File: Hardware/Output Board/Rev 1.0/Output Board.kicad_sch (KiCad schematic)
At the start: 85 parts, among them J1 Prog, J2 SD_Card, J3 Audio L, J4 Audio R, J5 VGA, J6 Conn_02x08_Odd_Even, J7 6502 Bus, U1 ICE40UP5K-SG48ITR50, U10 74HC138, U11 74HC138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

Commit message: Output Board schematic complete
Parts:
- C1, C10, C13, C14, C16, C17, C18, C19, C3, C4, C5, C6, C9: footprint Capacitor_SMD:C_0603_1608Metric -> Capacitor_SMD:C_0805_2012Metric; LCSC (none) -> C49678
- C11, C12, C2, C24, C25, C7, C8: footprint Capacitor_SMD:C_0603_1608Metric -> Capacitor_SMD:C_0805_2012Metric; LCSC (none) -> C1779
- C15, C21: footprint Capacitor_SMD:C_0603_1608Metric -> Capacitor_SMD:C_0805_2012Metric; LCSC (none) -> C1733
- C20: value 1u -> 1uF; footprint Capacitor_SMD:C_0603_1608Metric -> Capacitor_SMD:C_0805_2012Metric; LCSC (none) -> C28323
- C22: footprint Capacitor_SMD:C_0603_1608Metric -> Capacitor_SMD:C_0805_2012Metric; LCSC (none) -> C377773
- C23: footprint Capacitor_SMD:C_0603_1608Metric -> Capacitor_SMD:C_0805_2012Metric; LCSC (none) -> C28323
- C26, C27, C28, C29: LCSC (none) -> C1713
- C31: footprint Capacitor_THT:C_Disc_D5.0mm_W2.5mm_P5.00mm -> Capacitor_SMD:C_0805_2012Metric
- J1, J5, JP1: now left out of the parts list
- J2: LCSC (none) -> C569097
- L1: LCSC (none) -> C92959
- R1, R2, R3: footprint Resistor_SMD:R_0603_1608Metric -> Resistor_SMD:R_0805_2012Metric; LCSC (none) -> C17414
- R10, R15: footprint Resistor_SMD:R_0603_1608Metric -> Resistor_SMD:R_0805_2012Metric; LCSC (none) -> C28636
- R11, R18, R26: footprint Resistor_SMD:R_0603_1608Metric -> Resistor_SMD:R_0805_2012Metric; LCSC (none) -> C17746
- R12, R19, R27: footprint Resistor_SMD:R_0603_1608Metric -> Resistor_SMD:R_0805_2012Metric; LCSC (none) -> C17476
- R13, R14, R20, R23, R4, R5, R6, R7, R8, R9: footprint Resistor_SMD:R_0603_1608Metric -> Resistor_SMD:R_0805_2012Metric; LCSC (none) -> C17713
- R16, R22, R28: footprint Resistor_SMD:R_0603_1608Metric -> Resistor_SMD:R_0805_2012Metric; LCSC (none) -> C17516
- R17, R25, R29: footprint Resistor_SMD:R_0603_1608Metric -> Resistor_SMD:R_0805_2012Metric; LCSC (none) -> C17667
- R21, R24: footprint Resistor_SMD:R_0603_1608Metric -> Resistor_SMD:R_0805_2012Metric; LCSC (none) -> C17837
- U1: LCSC (none) -> C2889329
- U10: footprint Package_DIP:DIP-16_W7.62mm_Socket_LongPads -> Package_SO:SOIC-16_3.9x9.9mm_P1.27mm
- U2: LCSC (none) -> C176912
- U3: LCSC (none) -> C2655473
- U4: LCSC (none) -> C543078
- U5: LCSC (none) -> C7859
- U6: LCSC (none) -> C146242
- U7: LCSC (none) -> C2456211
- U8: LCSC (none) -> C500759
- U9: LCSC (none) -> C41348078
- X1: LCSC (none) -> C45324566

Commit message: Working on Output Board
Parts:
- J1: value Prog -> PROG
- J2: value SD_Card -> SD CARD
- J3: value Audio L -> AUDIO L
- J4: value Audio R -> AUDIO R
- JP1: value Flash Enable -> FLASH EN
- U2: footprint Package_SO:TSSOP-14_4.4x5mm_P0.65mm -> Package_SO:SOIC-14_3.9x8.7mm_P1.27mm
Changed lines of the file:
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@@
 	)
 	(global_label "SYSCLK"
-		(shape output)
+		(shape input)
 		(at 76.2 44.45 0)
 		(effects
@@
 			)
 		)
-		(property "Value" "Prog"
+		(property "Value" "PROG"
 			(at 129.54 53.34 0)
 			(effects
@@
 			)
 		)
-		(property "Value" "Flash Enable"
+		(property "Value" "FLASH EN"
 			(at 228.6 21.7424 0)
 			(effects
@@
 			)
 		)
-		(property "Value" "Audio R"
+		(property "Value" "AUDIO R"
 			(at 304.546 138.684 0)
 			(effects
@@
 			)
 		)
-		(property "Footprint" "Package_SO:TSSOP-14_4.4x5mm_P0.65mm"
+		(property "Footprint" "Package_SO:SOIC-14_3.9x8.7mm_P1.27mm"
 			(at 264.16 25.4 0)
 			(effects
@@
 			)
 		)
-		(property "Value" "SD_Card"
+		(property "Value" "SD CARD"
 			(at 316.23 75.5904 0)
 			(effects
@@
 			)
 		)
-		(property "Value" "Audio L"
+		(property "Value" "AUDIO L"
 			(at 304.546 124.714 0)
 			(effects
@@
 			)
 		)
-		(property "Footprint" "Package_SO:TSSOP-14_4.4x5mm_P0.65mm"
+		(property "Footprint" "Package_SO:SOIC-14_3.9x8.7mm_P1.27mm"
 			(at 294.64 34.29 0)
 			(effects
@@
 			)
 		)
-		(property "Footprint" "Package_SO:TSSOP-14_4.4x5mm_P0.65mm"
+		(property "Footprint" "Package_SO:SOIC-14_3.9x8.7mm_P1.27mm"
 			(at 245.11 46.99 0)
 			(effects
@@
 			)
 		)
-		(property "Footprint" "Package_SO:TSSOP-14_4.4x5mm_P0.65mm"
+		(property "Footprint" "Package_SO:SOIC-14_3.9x8.7mm_P1.27mm"
 			(at 245.11 33.02 0)
 			(effects
@@
 			)
 		)
-		(property "Footprint" "Package_SO:TSSOP-14_4.4x5mm_P0.65mm"
+		(property "Footprint" "Package_SO:SOIC-14_3.9x8.7mm_P1.27mm"
 			(at 264.16 39.37 0)
 			(effects

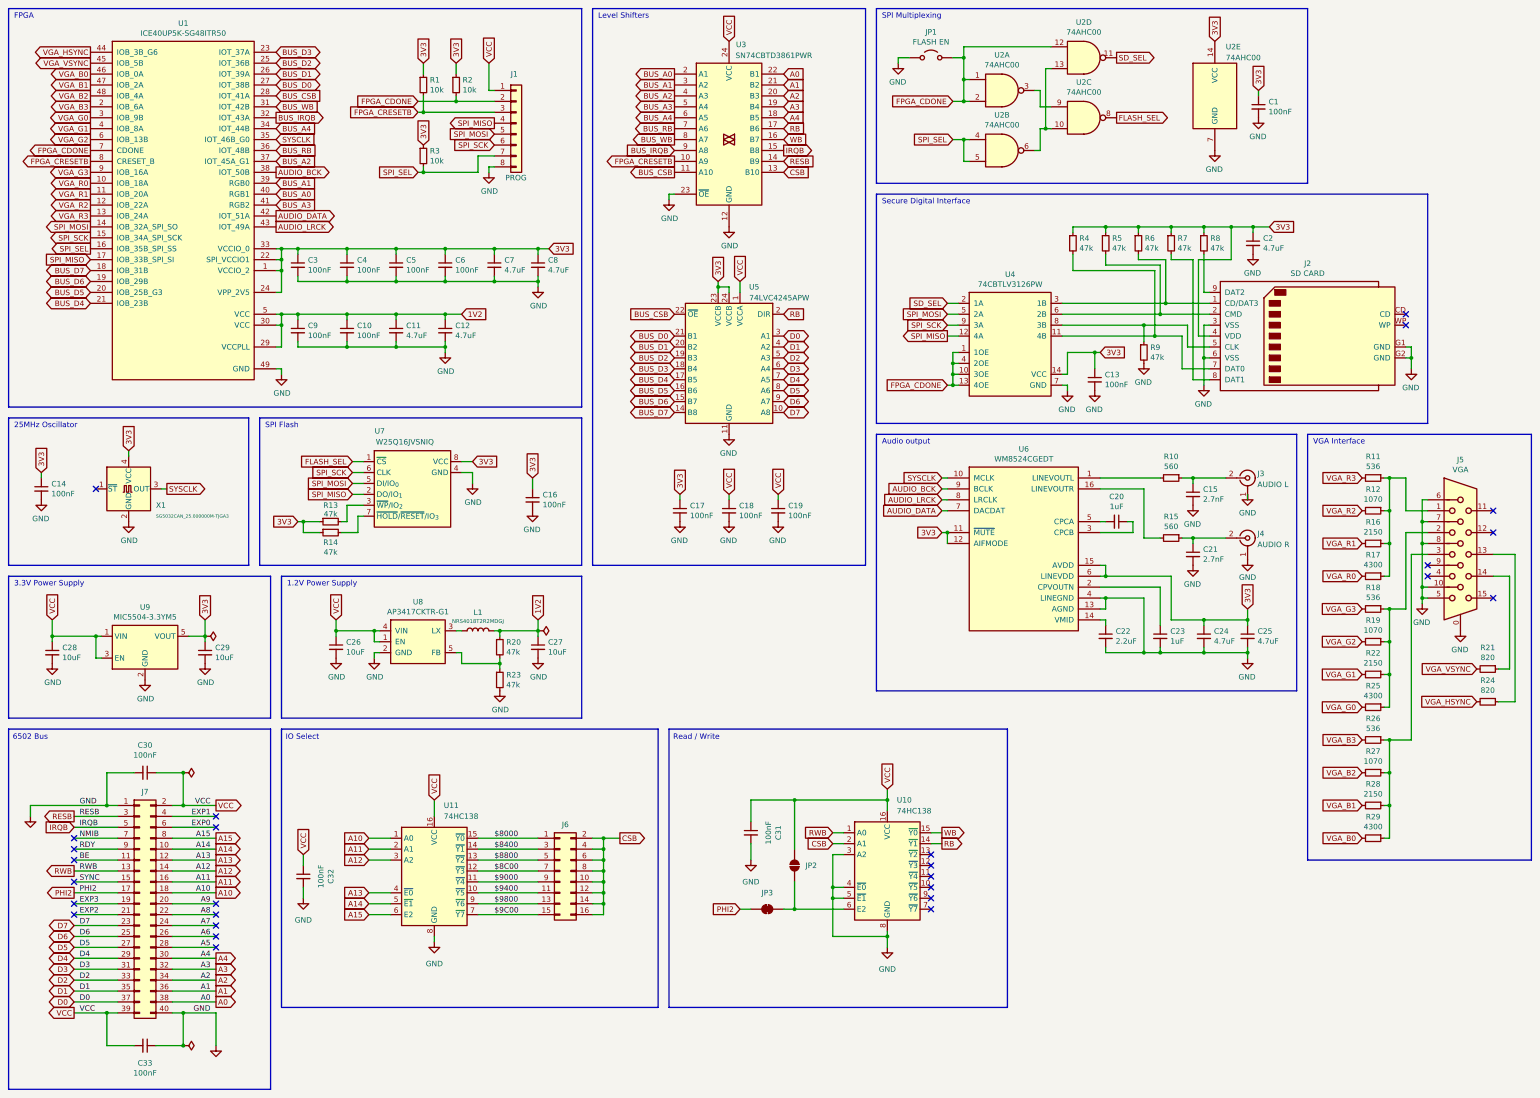
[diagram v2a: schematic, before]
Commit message: Begin Output Board Redesign
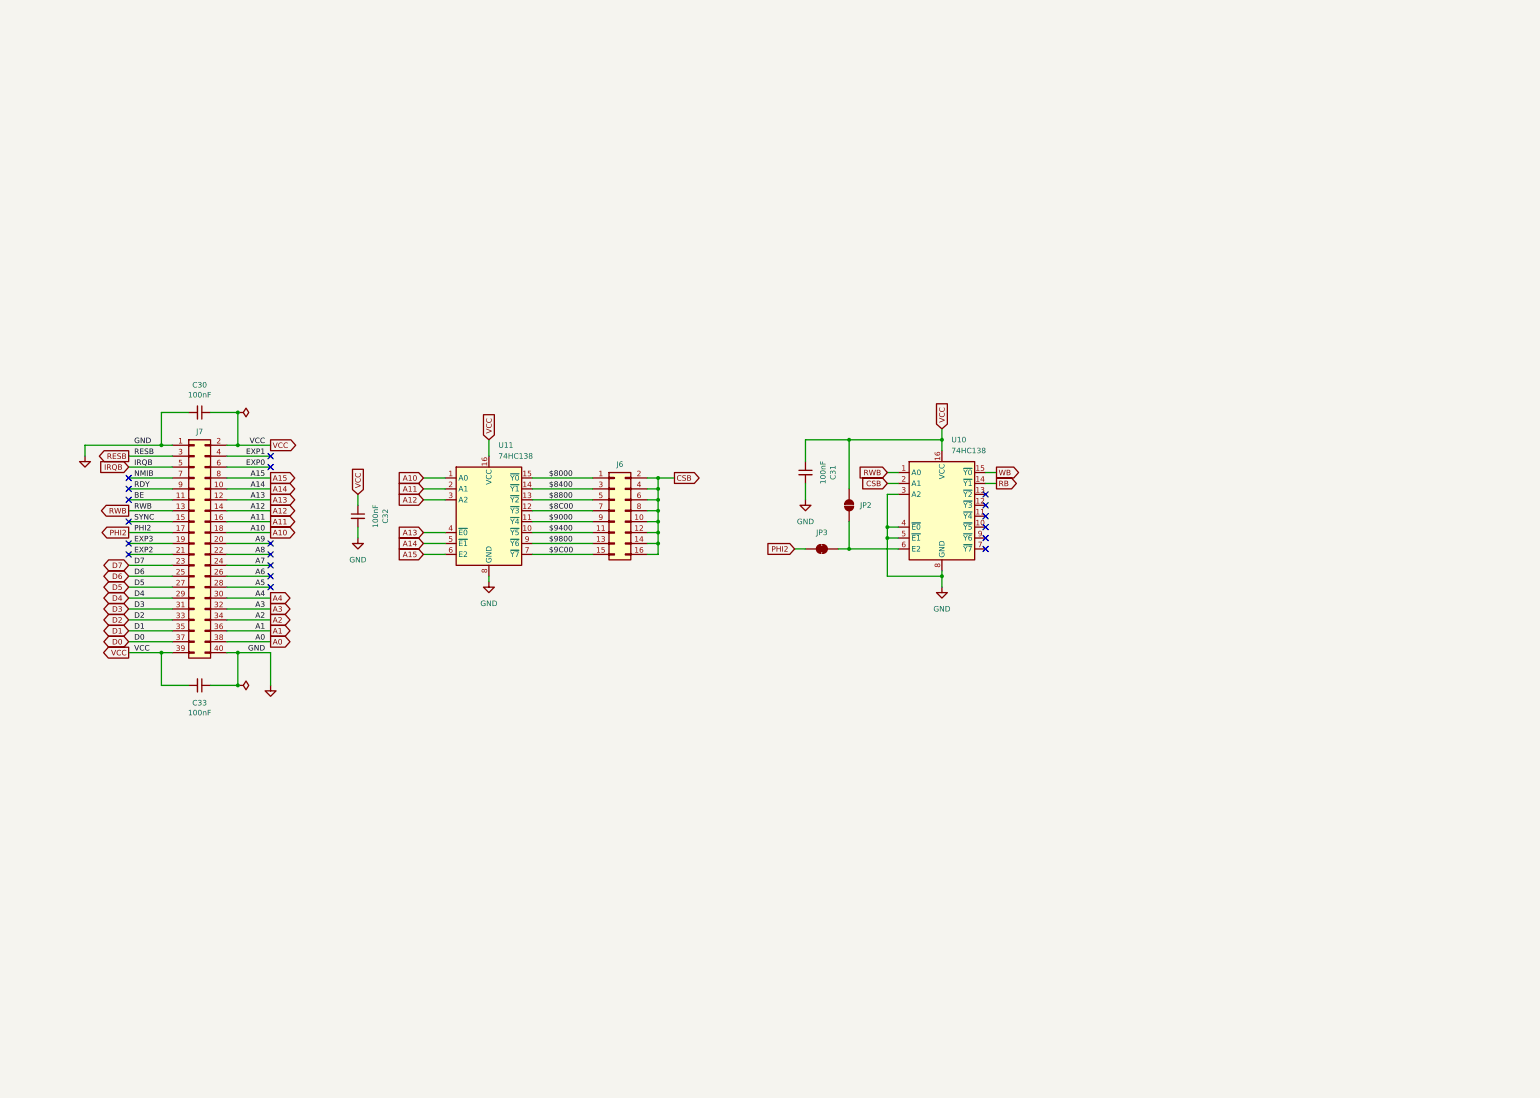
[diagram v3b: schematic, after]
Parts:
- removed C1, C10, C13, C14, C16, C17, C18, C19, C3, C4, C5, C6, C9: 100nF, Capacitor_SMD:C_0805_2012Metric, symbol Device:C_Small
- removed C11, C12, C2, C24, C25, C7, C8: 4.7uF, Capacitor_SMD:C_0805_2012Metric, symbol Device:C_Small
- removed C15, C21: 2.7nF, Capacitor_SMD:C_0805_2012Metric, symbol Device:C_Small
- removed C20, C23: 1uF, Capacitor_SMD:C_0805_2012Metric, symbol Device:C_Small
- removed C22: 2.2uF, Capacitor_SMD:C_0805_2012Metric, symbol Device:C_Small
- removed C26, C27, C28, C29: 10uF, Capacitor_SMD:C_0805_2012Metric, symbol Device:C_Small
- removed J1: PROG, Connector_PinHeader_2.54mm:PinHeader_1x08_P2.54mm_Vertical, symbol Connector_Generic:Conn_01x08
- removed J2: SD CARD, 6502 Parts:10067847-001RLF, symbol 6502 Parts:SD Card
- removed J3: AUDIO L, 6502 Parts:SWITCHCRAFT_PJRAN1X1U02X, symbol 6502 Parts:PJRAN1X1U02X
- removed J4: AUDIO R, 6502 Parts:SWITCHCRAFT_PJRAN1X1U02X, symbol 6502 Parts:PJRAN1X1U02X
- removed J5: VGA, Connector_Dsub:DSUB-15-HD_Socket_Horizontal_P2.29x1.90mm_EdgePinOffset3.03mm_Housed_MountingHolesOffset4.94mm, symbol Connector:DE15_Socket_HighDensity_MountingHoles
- removed JP1: FLASH EN, Connector_PinHeader_2.54mm:PinHeader_1x02_P2.54mm_Vertical, symbol Jumper:Jumper_2_Open
- removed L1: NRS4018T2R2MDGJ, Inductor_SMD:L_Bourns-SRN4018, symbol Device:L
- removed R1, R2, R3: 10k, Resistor_SMD:R_0805_2012Metric, symbol Device:R_Small
- removed R10, R15: 560, Resistor_SMD:R_0805_2012Metric, symbol Device:R_Small
- removed R11, R18, R26: 536, Resistor_SMD:R_0805_2012Metric, symbol Device:R_Small
- removed R12, R19, R27: 1070, Resistor_SMD:R_0805_2012Metric, symbol Device:R_Small
- removed R13, R14, R20, R23, R4, R5, R6, R7, R8, R9: 47k, Resistor_SMD:R_0805_2012Metric, symbol Device:R_Small
- removed R16, R22, R28: 2150, Resistor_SMD:R_0805_2012Metric, symbol Device:R_Small
- removed R17, R25, R29: 4300, Resistor_SMD:R_0805_2012Metric, symbol Device:R_Small
- removed R21, R24: 820, Resistor_SMD:R_0805_2012Metric, symbol Device:R_Small
- removed U1: ICE40UP5K-SG48ITR50, Package_DFN_QFN:QFN-48-1EP_7x7mm_P0.5mm_EP5.3x5.3mm, symbol 6502 Parts:ICE40UP5K-SG48ITR50
- removed U2: 74AHC00, Package_SO:SOIC-14_3.9x8.7mm_P1.27mm, symbol 74xx:74HC00
- removed U3: SN74CBTD3861PWR, Package_SO:TSSOP-24_4.4x7.8mm_P0.65mm, symbol 74xx:74CBTLV3861
- removed U4: 74CBTLV3126PW, Package_SO:TSSOP-14_4.4x5mm_P0.65mm, symbol 6502 Parts:74CBTLV3126PW
- removed U5: 74LVC4245APW, Package_SO:TSSOP-24_4.4x7.8mm_P0.65mm, symbol Logic_LevelTranslator:SN74AVC8T245PW
- removed U6: WM8524CGEDT, Package_SO:TSSOP-16_4.4x5mm_P0.65mm, symbol 6502 Parts:WM8524CGEDT
- removed U7: W25Q16JVSNIQ, Package_SO:SOIC-8_3.9x4.9mm_P1.27mm, symbol 6502 Parts:W25Q16JVSNIQ
- removed U8: AP3417CKTR-G1, Package_TO_SOT_SMD:SOT-23-5, symbol 6502 Parts:AP3417CKTR-G1
- removed U9: MIC5504-3.3YM5, Package_TO_SOT_SMD:SOT-23-5, symbol Regulator_Linear:MIC5504-3.3YM5
- removed X1: SG5032CAN_25.000000M-TJGA3, Oscillator:Oscillator_SMD_SeikoEpson_SG8002LB-4Pin_5.0x3.2mm, symbol Oscillator:SG-5032CAN
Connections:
- no-connect marks 27 -> 19
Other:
- note removed: "1.2V Power Supply"
- note removed: "25MHz Oscillator"
- note removed: "3.3V Power Supply"
- note removed: "Audio output"
- note removed: "FPGA"
- note removed: "Level Shifters"
- note removed: "SPI Flash"
- note removed: "SPI Multiplexing"
- note removed: "Secure Digital Interface"
- note removed: "VGA Interface"
- moved on the sheet: C30, C31, C32, C33, J6, J7, JP2, JP3, U10, U11

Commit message: Working on Output Board
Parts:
- removed C31: 100nF, Capacitor_SMD:C_0805_2012Metric, symbol Device:C_Small
- added C1: 1uF, Capacitor_SMD:C_0805_2012Metric, symbol Device:C
- added C10, C4, C7, C9: 100nF, Capacitor_SMD:C_0805_2012Metric, symbol Device:C
- added C2, C3: 2.2nF, Capacitor_SMD:C_0805_2012Metric, symbol Device:C
- added D1: D_Schottky, Diode_THT:D_DO-35_SOD27_P7.62mm_Horizontal, symbol Device:D_Schottky
- added FB1: BLM41PG600SN1L, Inductor_SMD:L_1806_4516Metric, symbol Device:FerriteBead
- added J1: VDD, Connector_JST:JST_XH_B2B-XH-A_1x02_P2.50mm_Vertical, symbol Connector_Generic:Conn_01x02
- added J2: AUDIO, 6502 Parts:SWITCHCRAFT_PJRAN1X1U02X, symbol 6502 Parts:PJRAN1X1U02X
- added J3: VIDEO, 6502 Parts:SWITCHCRAFT_PJRAN1X1U04X, symbol 6502 Parts:PJRAN1X1U04X
- added J4: INT Select, Connector_PinHeader_2.54mm:PinHeader_1x03_P2.54mm_Vertical, symbol Connector_Generic:Conn_01x03
- added JP1: SolderJumper_2_Bridged, Jumper:SolderJumper-2_P1.3mm_Bridged_RoundedPad1.0x1.5mm, symbol Jumper:SolderJumper_2_Bridged
- added Q1: 2N4401, Package_TO_SOT_THT:TO-92_HandSolder, symbol Simulation_SPICE:NPN
- added R1: 1k, Resistor_SMD:R_0805_2012Metric, symbol Device:R
- added R2: 470, Resistor_SMD:R_0805_2012Metric, symbol Device:R
- added R3: 75, Resistor_SMD:R_0805_2012Metric, symbol Device:R
- added U1: 6581, Socket:DIP_Socket-28_W11.9mm_W12.7mm_W15.24mm_W17.78mm_W18.5mm_3M_228-1277-00-0602J, symbol 6502 Parts:6581
- added U2: Pico9918A, Socket:DIP_Socket-40_W11.9mm_W12.7mm_W15.24mm_W17.78mm_W18.5mm_3M_240-1280-00-0602J, symbol 6502 Parts:Pico9918A
- C5: renamed from C30; symbol Device:C_Small -> Device:C
- C6: renamed from C33; symbol Device:C_Small -> Device:C
- C8: renamed from C32; symbol Device:C_Small -> Device:C
- renumbered J6 to J5, J7 to J6, U10 to U3, U11 to U4
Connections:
- net A0: now also U1.9 (A0), U2.13 (MODE)
- net A1: now also U1.10 (A1)
- net A2: now also U1.11 (A2)
- net A3: now also U1.12 (A3)
- net A4: now also U1.13 (A4)
- net D0: now also U1.15 (D0), U2.17 (CD7)
- net D1: now also U1.16 (D1), U2.18 (CD6)
- net D2: now also U1.17 (D2), U2.19 (CD5)
- net D3: now also U1.18 (D3), U2.20 (CD4)
- net D4: now also U1.19 (D4), U2.21 (CD3)
- net D5: now also U1.20 (D5), U2.22 (CD2)
- net D6: now also U1.21 (D6), U2.23 (CD1)
- net D7: now also U1.22 (D7), U2.24 (CD0)
- net GND: now also C10.2, C4.2, C7.2, C9.2, J1.2 (Pin_2), J2.1 (Ext), J3.1 (Ext), R1.2, R2.2, R3.2, U1.14 (GND), U2.12 (VSS)
- net IRQB: now also J4.1 (Pin_1)
- net NMIB: now also J4.3 (Pin_3)
- net PHI2: now also U1.6 (PHI2)
- net RB: now also U2.15 (~{CSR})
- net RESB: now also U1.5 (~{RESET}), U2.34 (~{RESET}/SYNC)
- net RWB: now also U1.7 (R/~{W})
- net VCC: now also C10.1, C7.1, C9.1, FB1.1, U1.25 (VCC), U2.33 (VCC)
- net WB: now also U2.14 (~{CSW})
- net CSB renamed CSBV
- net CSBV: no longer J5.10 (Pin_10), J5.14 (Pin_14), J5.2 (Pin_2), J5.6 (Pin_6)
- new net: C1.2, J2.2 (In)
- new net: J1.1 (Pin_1), U1.28 (VDD)
- new net: C4.1, FB1.2, Q1.1 (C)
- new net: C3.1, U1.4 (CAP2B)
- new net: C3.2, U1.3 (CAP2A)
- new net: D1.2 (A), J4.2 (Pin_2), JP1.2 (B)
- new net: C2.2, U1.1 (CAP1A)
- new net: C2.1, U1.2 (CAP1B)
- new net: J3.2 (In), Q1.3 (E), R3.1
- new net AUDIO: C1.1, R1.1, U1.27 (OUT)
- new net CSBA: J5.10 (Pin_10), J5.14 (Pin_14), J5.2 (Pin_2), J5.6 (Pin_6), U1.8 (~{CS})
- new net INTB: D1.1 (K), JP1.1 (A), U2.16 (~{INT})
- new net VIDEO: Q1.2 (B), R2.1, U2.36 (COMVID)
- no-connect marks 19 -> 23
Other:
- moved on the sheet: C5, C6, C8, J5, J6, JP2, JP3, U3, U4

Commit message: Working on Output Board
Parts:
- added J3: VGA, Connector_FFC-FPC:Hirose_FH12-12S-0.5SH_1x12-1MP_P0.50mm_Horizontal, symbol Connector_Generic:Conn_01x12
- added J4: VGA, Connector_Dsub:DSUB-15-HD_Socket_Horizontal_P2.29x1.90mm_EdgePinOffset3.03mm_Housed_MountingHolesOffset4.94mm, symbol Connector:DE15_Socket_HighDensity_MountingHoles
- renumbered J3 to J5, J4 to J6, J5 to J7, J6 to J8, U2 to U1, U1 to U2
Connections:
- net GND: now also J3.10 (Pin_10), J3.2 (Pin_2), J3.4 (Pin_4), J3.6 (Pin_6), J3.8 (Pin_8), J4.0
- new net: J3.3 (Pin_3), J4.1
- new net: J3.9 (Pin_9), J4.13
- new net: J3.11 (Pin_11), J4.14
- new net: J3.5 (Pin_5), J4.2
- new net: J3.7 (Pin_7), J4.3
- no-connect marks 23 -> 35
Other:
- moved on the sheet: D1, J6, JP1, U1

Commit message: Finish Output Board
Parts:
- removed C4: 100nF, Capacitor_SMD:C_0805_2012Metric, symbol Device:C
- removed FB1: BLM41PG600SN1L, Inductor_SMD:L_1806_4516Metric, symbol Device:FerriteBead
- removed J3: VGA, Connector_FFC-FPC:Hirose_FH12-12S-0.5SH_1x12-1MP_P0.50mm_Horizontal, symbol Connector_Generic:Conn_01x12
- removed J4: VGA, Connector_Dsub:DSUB-15-HD_Socket_Horizontal_P2.29x1.90mm_EdgePinOffset3.03mm_Housed_MountingHolesOffset4.94mm, symbol Connector:DE15_Socket_HighDensity_MountingHoles
- removed J5: VIDEO, 6502 Parts:SWITCHCRAFT_PJRAN1X1U04X, symbol 6502 Parts:PJRAN1X1U04X
- removed Q1: 2N4401, Package_TO_SOT_THT:TO-92_HandSolder, symbol Simulation_SPICE:NPN
- removed R2: 470, Resistor_SMD:R_0805_2012Metric, symbol Device:R
- removed R3: 75, Resistor_SMD:R_0805_2012Metric, symbol Device:R
- U1: footprint Socket:DIP_Socket-40_W11.9mm_W12.7mm_W15.24mm_W17.78mm_W18.5mm_3M_240-1280-00-0602J -> Package_DIP:DIP-40_W15.24mm_LongPads
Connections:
- net VIDEO: no longer names the net of U1.36 (COMVID)
- no-connect marks 35 -> 23
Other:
- moved on the sheet: C1, J2, R1

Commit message: Production fixes
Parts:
- U2: now left out of the parts list
- U3: now in the parts list
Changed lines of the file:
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@@
 		(unit 1)
 		(exclude_from_sim no)
-		(in_bom no)
+		(in_bom yes)
 		(on_board yes)
 		(dnp no)
@@
 		(unit 1)
 		(exclude_from_sim no)
-		(in_bom yes)
-		(on_board yes)
-		(dnp no)
+		(in_bom no)
+		(on_board yes)
+		(dnp no)
